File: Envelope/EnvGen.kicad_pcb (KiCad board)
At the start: 2 copper layers, 36 parts, among them J1 Input, J2 Output, J3 Power, Q1 BC817, Q2 BC817, Q3 BC817, U1 NE555, U2 LM324A

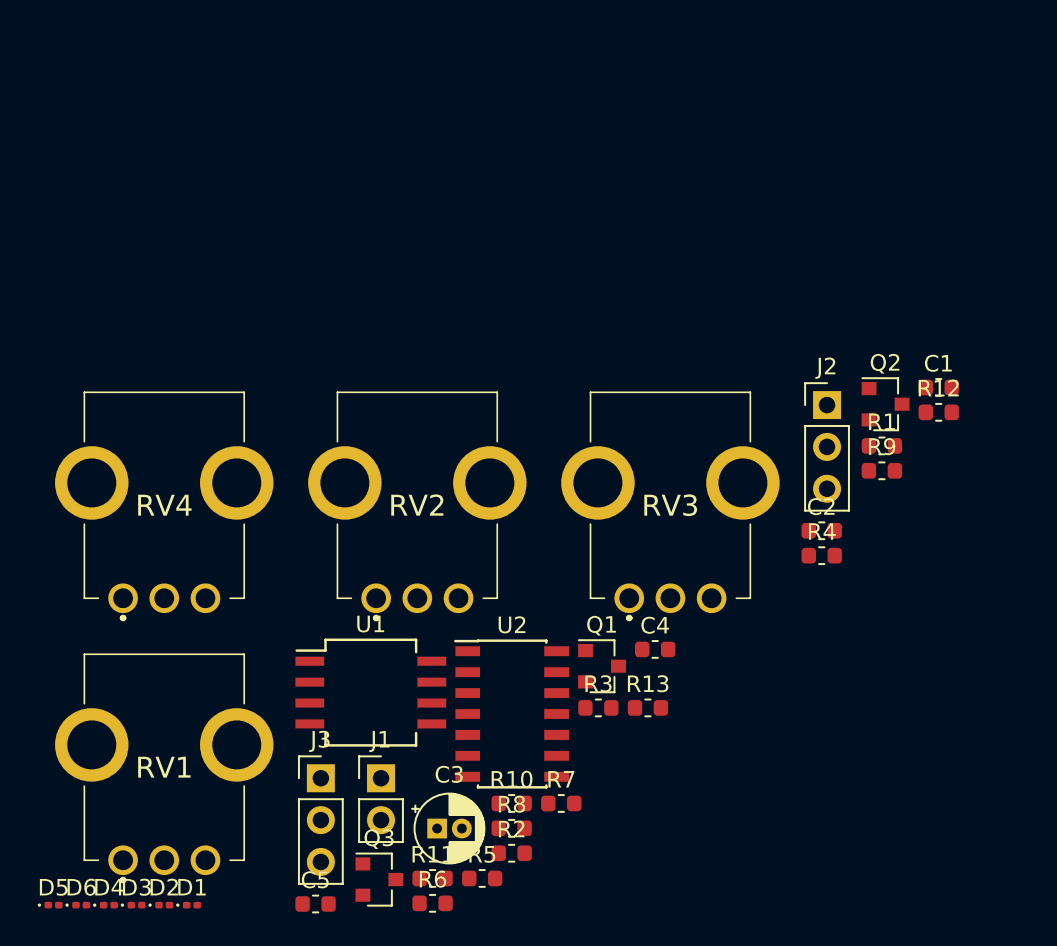
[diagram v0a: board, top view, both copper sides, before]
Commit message: Изменены библиотеки. Добавлинны библиотеки примененные в проекте локально. Добавленны заготовки для печатных плат. Добавленны 3D модели компоненток.
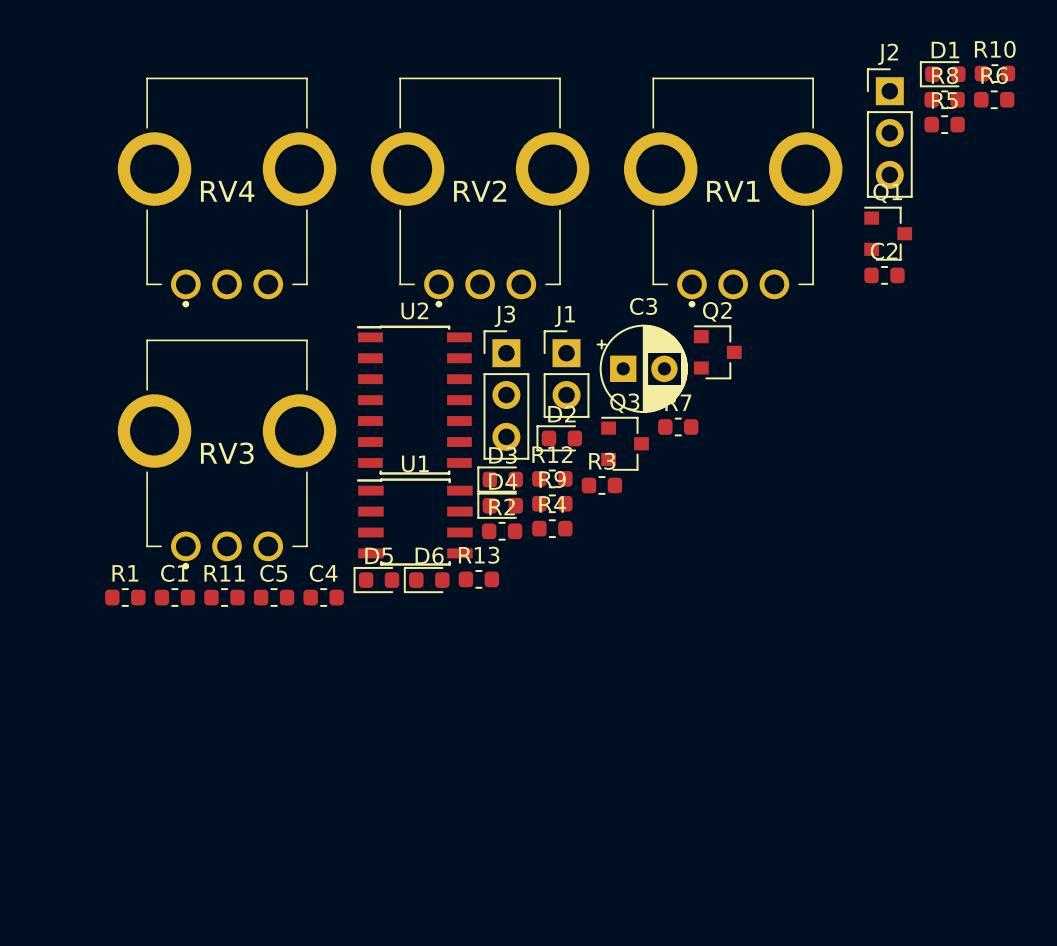
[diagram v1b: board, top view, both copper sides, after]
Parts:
- C1, C2, C4, C5: footprint Capacitor_SMD:C_0603_1608Metric -> footprint:c0603
- C3: footprint Capacitor_THT:CP_Radial_D4.0mm_P1.50mm -> footprint:cp_5x2_5
- D1, D2, D3, D4, D5, D6: footprint Diode_SMD:D_0201_0603Metric -> footprint:d0603
- J1: footprint Connector_PinHeader_2.54mm:PinHeader_1x02_P2.54mm_Vertical -> footprint:pls1x02
- J2, J3: footprint Connector_PinHeader_2.54mm:PinHeader_1x03_P2.54mm_Vertical -> footprint:pls1x03
- Q1, Q2, Q3: footprint Package_TO_SOT_SMD:SOT-23 -> footprint:SOT-23
- R1, R10, R11, R12, R13, R2, R3, R4, R5, R6, R7, R8, R9: footprint Resistor_SMD:R_0603_1608Metric -> footprint:r0603
- RV1, RV2, RV3, RV4: footprint R0409N:PTV09A4020FB103 -> footprint:R0904N
- U1: footprint Package_SO:SO-8_5.3x6.2mm_P1.27mm -> footprint:soic-8
- U2: footprint Package_SO:SOIC-14_3.9x8.7mm_P1.27mm -> footprint:soic-14
- moved D1 68.1 mm to (164.3, 63.0)
- moved R6 59.5 mm to (167.3, 64.6)
- moved R5 53.7 mm to (164.3, 66.1)
- moved R10 53.1 mm to (167.3, 63.0)
- moved R8 51.4 mm to (164.3, 64.6)
- moved RV1 49.1 mm to (151.4, 70.2)
- moved C1 48.1 mm to (117.5, 94.8)
- moved R1 46.8 mm to (114.5, 94.8)
- moved D2 37.2 mm to (141.0, 85.1)
- moved D3 34.1 mm to (137.4, 87.6)
- moved D4 34.0 mm to (137.4, 89.2)
- moved Q1 31.5 mm to (160.8, 72.7)
- moved Q3 30.4 mm to (144.9, 85.5)
- moved C3 30.1 mm to (144.8, 80.9)
- moved D6 28.9 mm to (133.0, 93.7)
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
